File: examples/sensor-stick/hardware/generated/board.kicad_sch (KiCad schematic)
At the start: 25 parts, among them J1 TYPE-C-31-M-12, U1 RP2040, U2 W25Q32JVSSIQ, U3 AMS1117-3.3, U4 AHT20, Y1 X322512MSB4SI

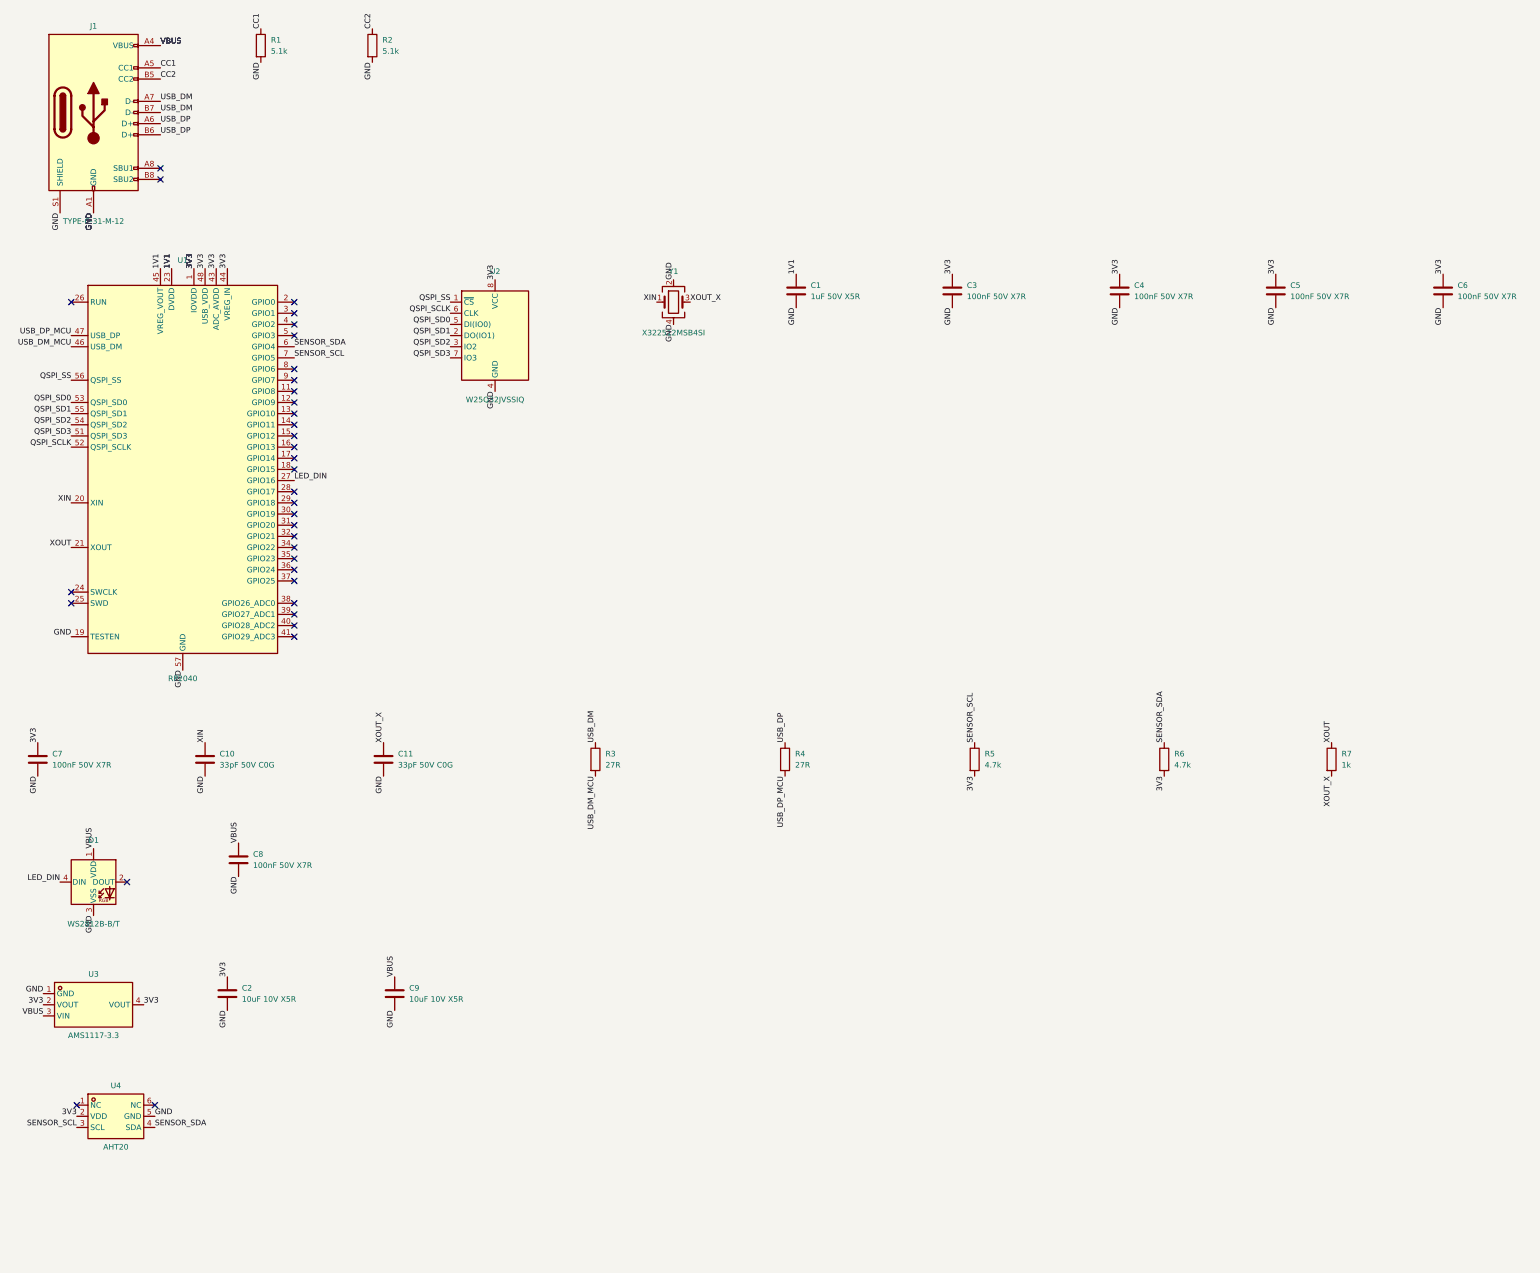
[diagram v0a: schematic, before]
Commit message: feat(examples): sensor-stick in blue, every part a real model, rebuilt
- case.colour = blue; nothing of any other product's look
- the regulator from KiCad's own library (flattened `extends`), the
  sensor and flash from LCSC's library with their models, the USB-C
  socket on KiCad's land pattern with LCSC's model, measured onto its
  drilled holes; the socket's mouth now faces the wall (it faced in)
- routed, DRC clean, every fit check passing, every part orderable
- the guide rebuilds it from scratch; its case study records each
  refusal of the first build, and the one no gate caught

Co-Authored-By: Claude Opus 5.5 <noreply@anthropic.com>
Claude-Session: https://claude.ai/code/session_01F145W5B7sgzWKAnWcVES4m
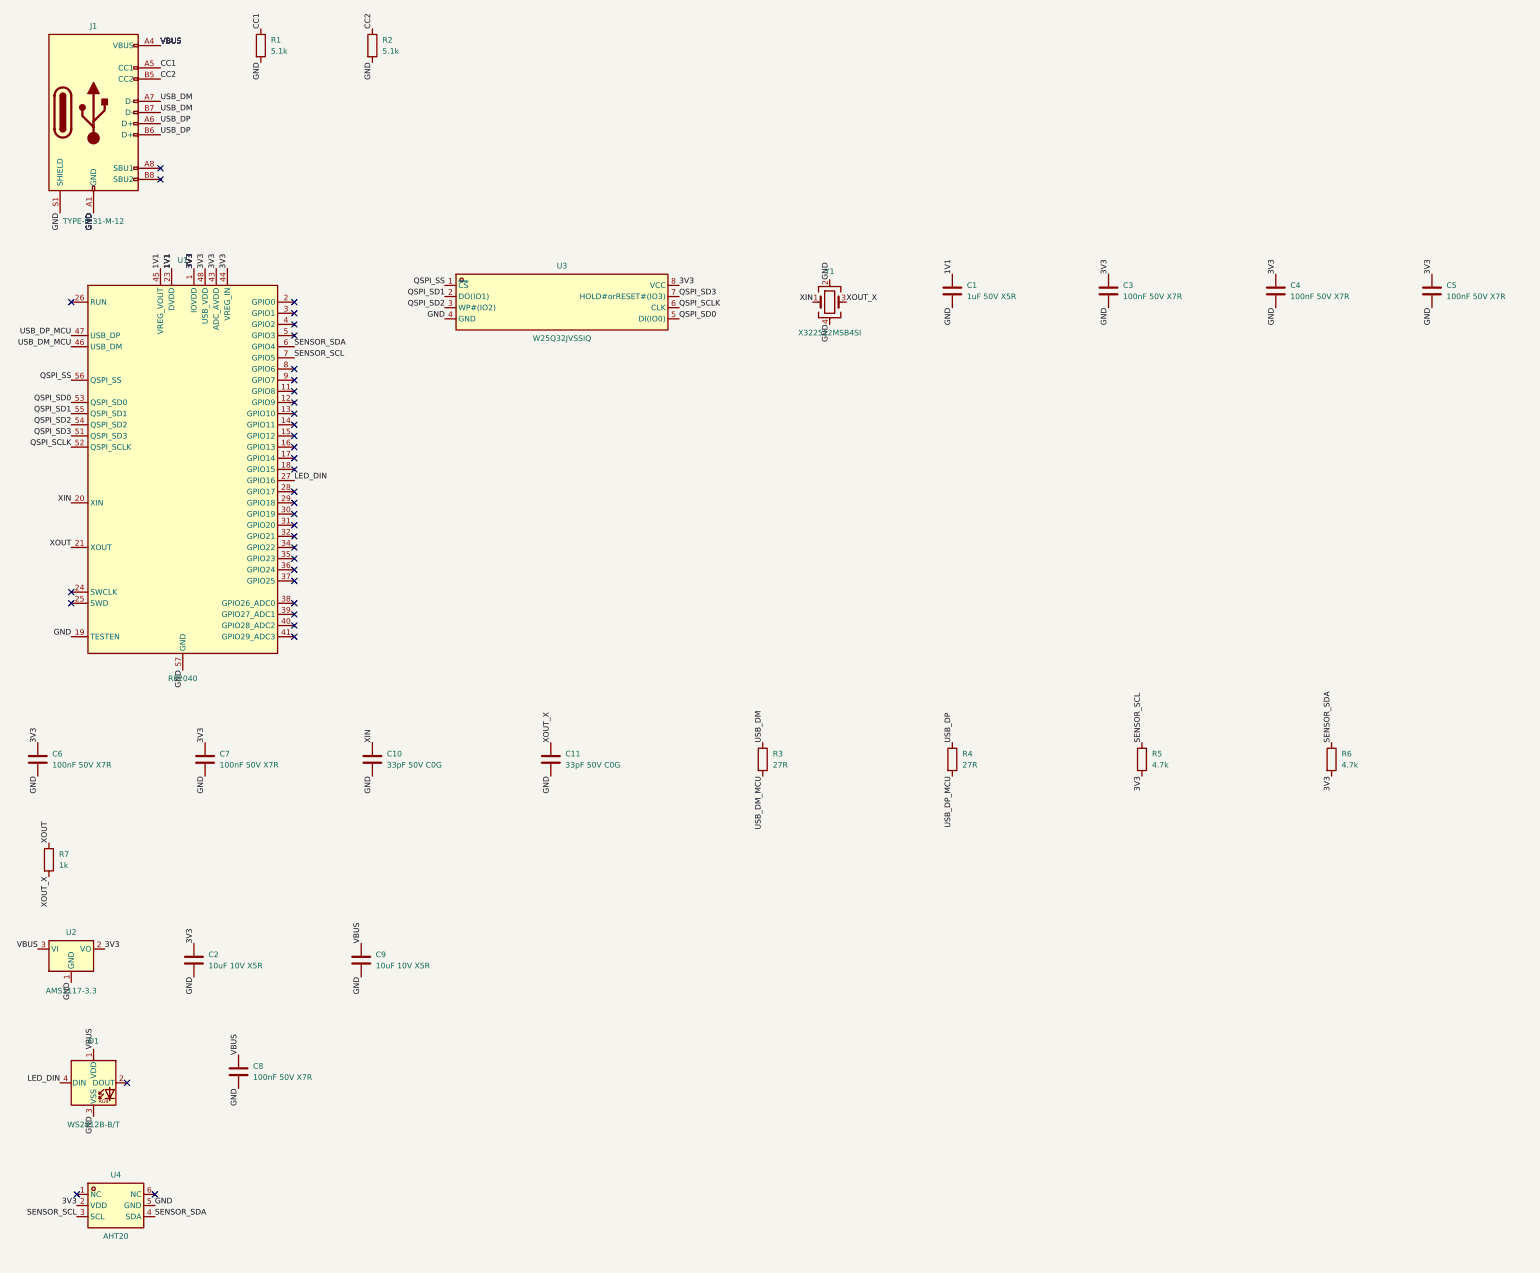
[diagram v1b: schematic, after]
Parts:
- U2: renamed from U3; footprint lcsc:SOT-223-3_L6.5-W3.4-P2.30-LS7.0-BR -> Package_TO_SOT_SMD:SOT-223-3_TabPin2; symbol lcsc:AMS1117-3.3 -> Regulator_Linear:AMS1117-3.3
- U3: renamed from U2; footprint Package_SO:SOIC-8_5.23x5.23mm_P1.27mm -> lcsc:SOIC-8_L5.3-W5.3-P1.27-LS8.0-BL; symbol Memory_Flash:W25Q32JVSS -> lcsc:W25Q32JVSSIQ_C179173
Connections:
- net 3V3: no longer U2.4 (VOUT)
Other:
- moved on the sheet: C1, C10, C11, C2, C3, C4, C5, C6, C7, C8, C9, D1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

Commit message: fix(examples): buffer the sensor stick's LED data line to 5 V
The WS2812B on 5 V reads high only above 0.7 x VDD = 3.5 V, and the
RP2040 drives 3.3 V: out of spec, though it often works on a bench. A
74AHCT1G125 on 5 V (TTL input, 2.0 V high) sits between them, with its
own decoupling; the MCU side keeps the LED_DIN net, so the firmware is
unchanged. No gate compares output levels with input thresholds, so the
case study gains a row: four of twenty-four caught only by review.

The board stays 26 x 79 mm at fill 0.66 and routes first time. Prices
now come from LCSC: $4.74 of parts per board at five. Renders refreshed.

Co-Authored-By: Claude Opus 5.5 <noreply@anthropic.com>
Claude-Session: https://claude.ai/code/session_01F145W5B7sgzWKAnWcVES4m
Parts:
- added C3: 100nF 50V X7R, Capacitor_SMD:C_0603_1608Metric, symbol Device:C
- added U4: SN74AHCT1G125DBVR, Package_TO_SOT_SMD:SOT-23-5, symbol 74xGxx:74AHCT1G125
- renumbered C9 to C10, C10 to C11, C11 to C12, C3 to C4, C4 to C5, C5 to C6, C6 to C7, C7 to C8, C8 to C9, U4 to U5
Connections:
- net GND: now also C3.2, U4.1, U4.3 (GND)
- net LED_DIN: now also U4.2; no longer D1.4 (DIN)
- net VBUS: now also C3.1, U4.5 (VCC)
- new net LED_DIN_5V: D1.4 (DIN), U4.4
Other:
- moved on the sheet: C9, D1, U5
